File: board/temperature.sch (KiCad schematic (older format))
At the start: 3 parts

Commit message: Comprehensive Schematic Review, Power LED
The schematic was reviewed. Components were selected. Fixed minor bugs
encountered during review. Debounced switches.

Added a power LED with a transistor that causes it to be normally-on.
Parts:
- U?: Part Number (none) -> MAX6675
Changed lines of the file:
@@
 $Descr A4 11693 8268
 encoding utf-8
-Sheet 9 26
+Sheet 2 26
 Title "K-Type Temperature Sensor"
 Date ""
@@
 U 1 1 52E6B9FE
 P 4850 3800
-AR Path="/52EEE819/52E6B9FE" Ref="C?"  Part="1"
-AR Path="/52E79355/52E6B9FE" Ref="C?"  Part="1"
 F 0 "C?" H 4850 3900 40  0000 L CNN
 F 1 "100nF" H 4856 3715 40  0000 L CNN
@@
 U 1 1 52E6BA13
 P 5200 4100
-AR Path="/52EEE819/52E6BA13" Ref="#PWR?"  Part="1"
-AR Path="/52E79355/52E6BA13" Ref="#PWR?"  Part="1"
 F 0 "#PWR?" H 5200 4100 30  0001 C CNN
 F 1 "GND" H 5200 4030 30  0001 C CNN
@@
 U 1 1 52E6BA4F
 P 4850 3400
-AR Path="/52EEE819/52E6BA4F" Ref="#PWR?"  Part="1"
-AR Path="/52E79355/52E6BA4F" Ref="#PWR?"  Part="1"
 F 0 "#PWR?" H 4850 3360 30  0001 C CNN
 F 1 "+3.3V" H 4850 3510 30  0000 C CNN
@@
 U 1 1 52E6BA82
 P 4850 4100
-AR Path="/52EEE819/52E6BA82" Ref="#PWR?"  Part="1"
-AR Path="/52E79355/52E6BA82" Ref="#PWR?"  Part="1"
 F 0 "#PWR?" H 4850 4100 30  0001 C CNN
 F 1 "GND" H 4850 4030 30  0001 C CNN
@@
 U 1 1 52E6BAA9
 P 5100 2700
-AR Path="/52EEE819/52E6BAA9" Ref="P?"  Part="1"
-AR Path="/52E79355/52E6BAA9" Ref="P?"  Part="1"
 F 0 "P?" V 5050 2700 40  0000 C CNN
 F 1 "CONN_2" V 5150 2700 40  0000 C CNN
@@
 U 1 1 52E6BBF9
 P 5650 3400
-AR Path="/52EEE819/52E6BBF9" Ref="U?"  Part="1"
-AR Path="/52E79355/52E6BBF9" Ref="U?"  Part="1"
 F 0 "U?" H 5500 3100 60  0000 C CNN
 F 1 "MAX6675" H 5650 3750 60  0000 C CNN
 F 2 "" H 5650 3400 60  0000 C CNN
 F 3 "" H 5650 3400 60  0000 C CNN
+F 4 "MAX6675" H 5650 3400 60  0001 C CNN "Part Number"
 	1    5650 3400
 	1    0    0    -1
@@
 U 1 1 52E6BC15
 P 5000 3350
-AR Path="/52EEE819/52E6BC15" Ref="#PWR?"  Part="1"
-AR Path="/52E79355/52E6BC15" Ref="#PWR?"  Part="1"
 F 0 "#PWR?" H 5000 3350 30  0001 C CNN
 F 1 "GND" H 5000 3280 30  0001 C CNN

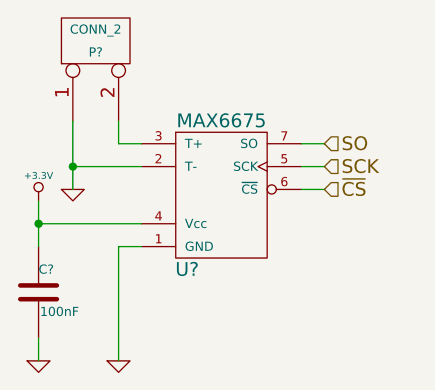
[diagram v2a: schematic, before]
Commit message: Fixed ERC Errors. Annotated all components.
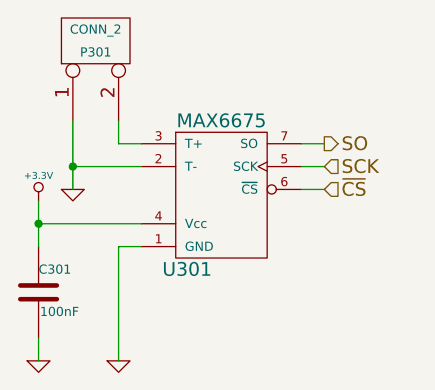
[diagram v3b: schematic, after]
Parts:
- gave numbers to parts that had none: 3
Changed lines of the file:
@@
 $Descr A4 11693 8268
 encoding utf-8
-Sheet 2 26
+Sheet 3 26
 Title "K-Type Temperature Sensor"
 Date ""
@@
 Text HLabel 6100 3350 2    60   Input ~ 0
 ~CS
-Text HLabel 6100 3150 2    60   Input ~ 0
+Text HLabel 6100 3150 2    60   Output ~ 0
 SO
 $Comp
-L C C?
+L C C201
 U 1 1 52E6B9FE
 P 4850 3800
-F 0 "C?" H 4850 3900 40  0000 L CNN
+AR Path="/52EEE819/52E6B9FE" Ref="C201"  Part="1"
+AR Path="/52E79355/52E6B9FE" Ref="C301"  Part="1"
+F 0 "C301" H 4850 3900 40  0000 L CNN
 F 1 "100nF" H 4856 3715 40  0000 L CNN
 F 2 "" H 4888 3650 30  0000 C CNN
@@
 $EndComp
 $Comp
-L GND #PWR?
+L GND #PWR0116
 U 1 1 52E6BA13
 P 5200 4100
-F 0 "#PWR?" H 5200 4100 30  0001 C CNN
+AR Path="/52EEE819/52E6BA13" Ref="#PWR0116"  Part="1"
+AR Path="/52E79355/52E6BA13" Ref="#PWR0120"  Part="1"
+F 0 "#PWR0120" H 5200 4100 30  0001 C CNN
 F 1 "GND" H 5200 4030 30  0001 C CNN
 F 2 "" H 5200 4100 60  0000 C CNN
@@
 	4850 3400 4850 3600
 $Comp
-L +3.3V #PWR?
+L +3.3V #PWR0117
 U 1 1 52E6BA4F
 P 4850 3400
-F 0 "#PWR?" H 4850 3360 30  0001 C CNN
+AR Path="/52EEE819/52E6BA4F" Ref="#PWR0117"  Part="1"
+AR Path="/52E79355/52E6BA4F" Ref="#PWR0121"  Part="1"
+F 0 "#PWR0121" H 4850 3360 30  0001 C CNN
 F 1 "+3.3V" H 4850 3510 30  0000 C CNN
 F 2 "" H 4850 3400 60  0000 C CNN
@@
 Connection ~ 4850 3500
 $Comp
-L GND #PWR?
+L GND #PWR0118
 U 1 1 52E6BA82
 P 4850 4100
-F 0 "#PWR?" H 4850 4100 30  0001 C CNN
+AR Path="/52EEE819/52E6BA82" Ref="#PWR0118"  Part="1"
+AR Path="/52E79355/52E6BA82" Ref="#PWR0122"  Part="1"
+F 0 "#PWR0122" H 4850 4100 30  0001 C CNN
 F 1 "GND" H 4850 4030 30  0001 C CNN
 F 2 "" H 4850 4100 60  0000 C CNN
@@
 	4850 4000 4850 4100
 $Comp
-L CONN_2 P?
+L CONN_2 P201
 U 1 1 52E6BAA9
 P 5100 2700
-F 0 "P?" V 5050 2700 40  0000 C CNN
+AR Path="/52EEE819/52E6BAA9" Ref="P201"  Part="1"
+AR Path="/52E79355/52E6BAA9" Ref="P301"  Part="1"
+F 0 "P301" V 5050 2700 40  0000 C CNN
 F 1 "CONN_2" V 5150 2700 40  0000 C CNN
 F 2 "" H 5100 2700 60  0000 C CNN
@@
 	6100 3350 6000 3350
 $Comp
-L MAX6675 U?
+L MAX6675 U201
 U 1 1 52E6BBF9
 P 5650 3400
-F 0 "U?" H 5500 3100 60  0000 C CNN
+AR Path="/52EEE819/52E6BBF9" Ref="U201"  Part="1"
+AR Path="/52E79355/52E6BBF9" Ref="U301"  Part="1"
+F 0 "U301" H 5500 3100 60  0000 C CNN
 F 1 "MAX6675" H 5650 3750 60  0000 C CNN
 F 2 "" H 5650 3400 60  0000 C CNN
@@
 $EndComp
 $Comp
-L GND #PWR?
+L GND #PWR0119
 U 1 1 52E6BC15
 P 5000 3350
-F 0 "#PWR?" H 5000 3350 30  0001 C CNN
+AR Path="/52EEE819/52E6BC15" Ref="#PWR0119"  Part="1"
+AR Path="/52E79355/52E6BC15" Ref="#PWR0123"  Part="1"
+F 0 "#PWR0123" H 5000 3350 30  0001 C CNN
 F 1 "GND" H 5000 3280 30  0001 C CNN
 F 2 "" H 5000 3350 60  0000 C CNN
